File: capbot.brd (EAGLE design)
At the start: 48.3 x 49 mm, 67 parts, among them J1 USBPCB, J2 USBPCB, J3 USBPCB

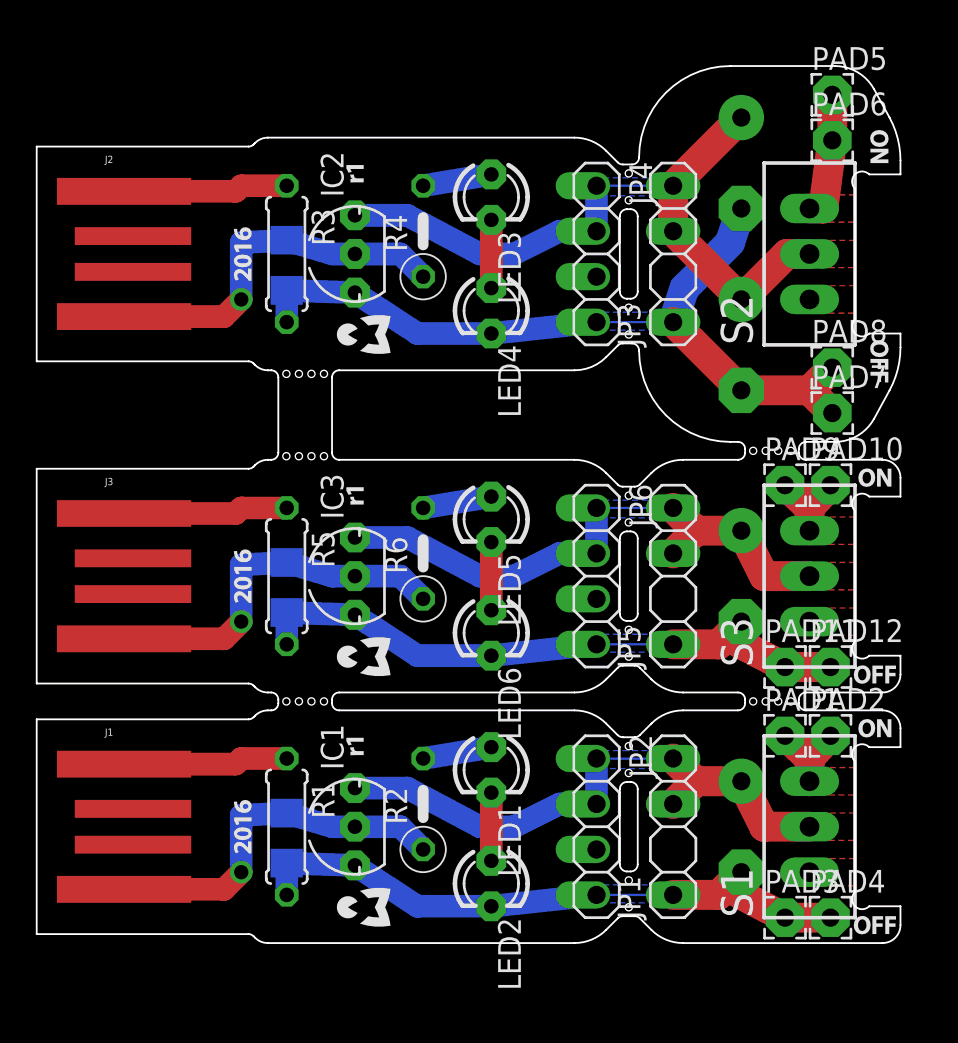
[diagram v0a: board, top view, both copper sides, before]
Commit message: Add power LED function.
With one added Zener diode, the top LED indicates that the device is powered, while both LEDs together still indicate that charging is completed.
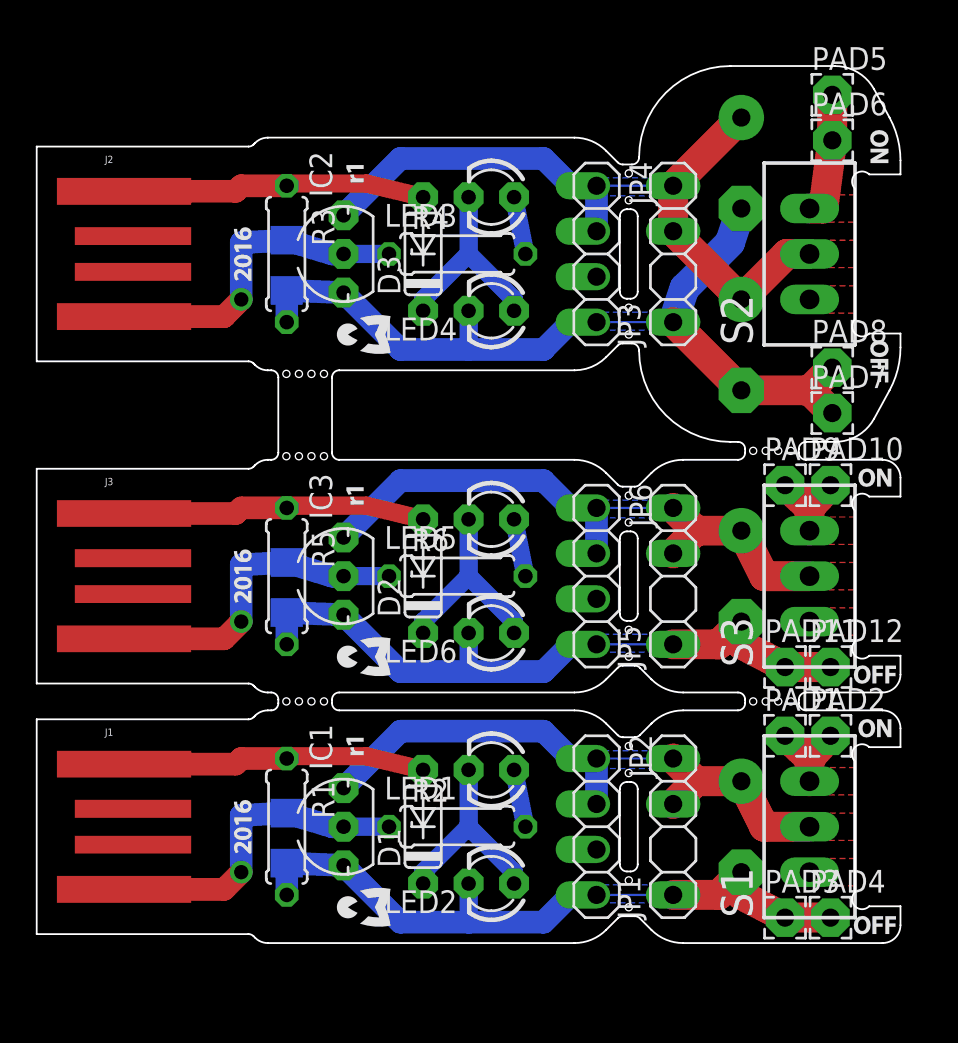
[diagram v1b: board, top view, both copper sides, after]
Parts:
- added D1, D2, D3: BZX55/6, cwpackage:DO35Z6
- R2, R4, R6: device resistor:0207/5V -> resistor:0207/7
- moved R4 2.29 mm to (23.5, 38.5), turned to 0 degrees
- moved R2 2.29 mm to (23.5, 6.50), turned to 0 degrees
- moved R6 2.29 mm to (23.5, 20.5), turned to 0 degrees
- moved IC1 0.64 mm to (17.1, 6.50)
- moved IC2 0.64 mm to (17.1, 38.5)
- moved IC3 0.64 mm to (17.1, 20.5)
- turned LED1 to 180 degrees
- turned LED2 to 180 degrees
- turned LED3 to 180 degrees
- turned LED4 to 180 degrees
- turned LED5 to 180 degrees
- turned LED6 to 180 degrees
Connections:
- net N$14: now also D3.A
- net N$19: now also D3.C
- net N$24: now also D2.A
- net N$29: now also D2.C
- net N$4: now also D1.A
- net N$9: now also D1.C
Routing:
- net N$24: track 9.22 -> 17.1 mm
- net N$4: track 9.22 -> 17.1 mm
- net N$14: track 9.22 -> 17.1 mm
- net N$9: track 3.81 -> 11.6 mm
- net N$29: track 3.81 -> 11.6 mm
- net N$19: track 3.81 -> 11.6 mm
- net N$11: track 44.5 -> 47.9 mm
- net N$1: track 35.0 -> 38.4 mm
- net N$21: track 35.0 -> 38.4 mm
- net N$26: track 20.9 -> 18.5 mm
- net N$6: track 20.9 -> 18.5 mm
- net N$16: track 20.9 -> 18.5 mm
- net N$22: track 32.7 -> 34.4 mm
- net N$2: track 32.7 -> 34.4 mm
- net N$12: track 39.3 -> 41.1 mm
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
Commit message: Get rid of a via by using an existing hole, and some other prettifications.
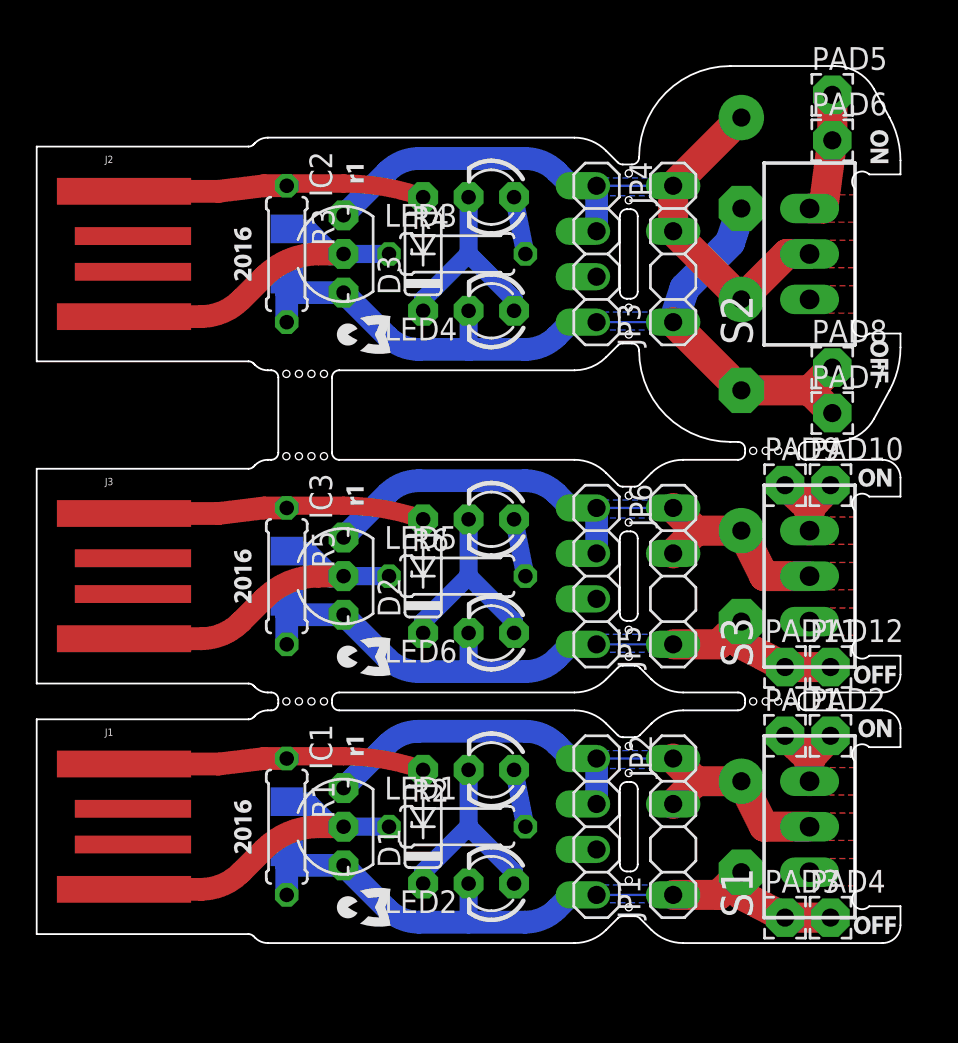
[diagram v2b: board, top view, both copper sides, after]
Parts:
- moved C7 0.64 mm to (14.0, 20.5)
- moved C2 0.63 mm to (14.0, 6.50)
- moved C4 0.63 mm to (14.0, 38.5)
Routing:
- net N$6: track 18.5 -> 20.3 mm, vias 1 -> 0
- net N$21: track 38.4 -> 39.4 mm
- net N$11: track 47.9 -> 48.9 mm
- net N$1: track 38.4 -> 39.4 mm
- net N$16: track 18.5 -> 19.5 mm, vias 1 -> 0
- net N$26: track 18.5 -> 19.5 mm, vias 1 -> 0

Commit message: Replace the zero-line-width silkscreen polygons by ones made for 0.15 mm line width.
Previously, they needlessly inflated the Gerber file size because Eagle apparently uses lines of the same width as the outline to fill them, resulting in ten-thousands of zero-width lines. The manufacturing also used a greater width (probably 0.15 mm), expanding the shapes.
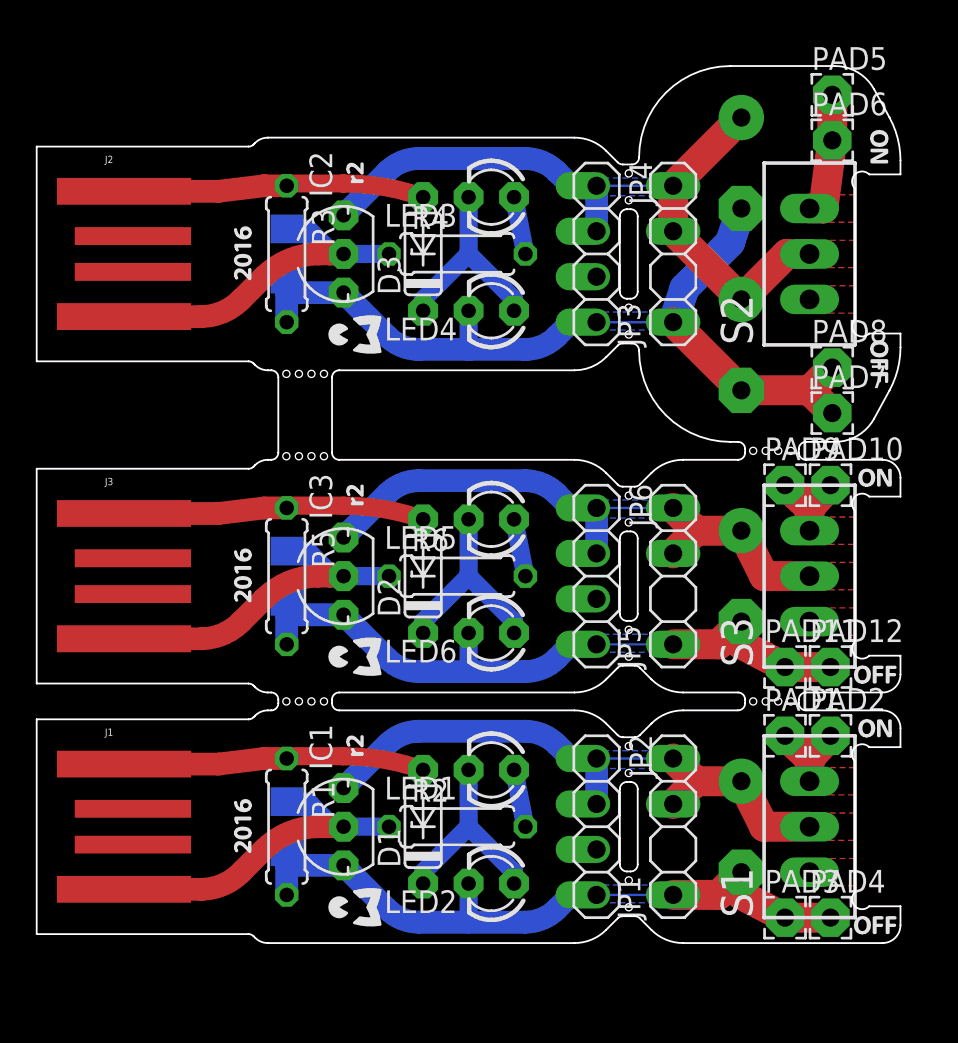
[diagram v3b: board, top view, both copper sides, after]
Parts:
- removed U$10, U$4, U$6: (no value), cwlogo:R1
- added U$22, U$23, U$24: (no value), cwlogo:R2
- moved U$1 0.49 mm to (17.8, 34.0)
- moved U$2 0.49 mm to (17.8, 2.00)
- moved U$8 0.49 mm to (17.8, 16.0)
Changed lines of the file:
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@@
 <element name="J2" library="SparkFun-Connectors" package="USB-A-PCB" value="USBPCB" x="5.08" y="38.5"/>
 <element name="C5" library="resistor" package="E5-10,5" value="" x="39.37" y="43.58" rot="MR270"/>
-<element name="U$1" library="cwlogo" package="CWLOGO-3" value="" x="18.27" y="34" rot="R90"/>
-<element name="U$2" library="cwlogo" package="CWLOGO-3" value="" x="18.27" y="2" rot="R90"/>
+<element name="U$1" library="cwlogo" package="CWLOGO-3" value="" x="17.78" y="34" rot="R90"/>
+<element name="U$2" library="cwlogo" package="CWLOGO-3" value="" x="17.78" y="2" rot="R90"/>
 <element name="U$3" library="cwlogo" package="2016" value="" x="12" y="6.5" rot="R90"/>
-<element name="U$4" library="cwlogo" package="R1" value="" x="18.27" y="11" rot="R90"/>
 <element name="U$5" library="cwlogo" package="2016" value="" x="12" y="38.5" rot="R90"/>
-<element name="U$6" library="cwlogo" package="R1" value="" x="18.27" y="43" rot="R90"/>
 <element name="C6" library="resistor" package="E5-10,5" value="" x="39.37" y="20.5" rot="MR270"/>
 <element name="S3" library="switch" package="TL3XPO" value="" x="43.18" y="20.5" rot="R90"/>
@@
 <element name="JP6" library="cwpinhead" package="1X04/OFFSETDOWN" value="" x="31.28" y="20.5" rot="R270"/>
 <element name="J3" library="SparkFun-Connectors" package="USB-A-PCB" value="USBPCB" x="5.08" y="20.5"/>
-<element name="U$8" library="cwlogo" package="CWLOGO-3" value="" x="18.27" y="16" rot="R90"/>
+<element name="U$8" library="cwlogo" package="CWLOGO-3" value="" x="17.78" y="16" rot="R90"/>
 <element name="U$9" library="cwlogo" package="2016" value="" x="12" y="20.5" rot="R90"/>
-<element name="U$10" library="cwlogo" package="R1" value="" x="18.27" y="25" rot="R90"/>
 <element name="U$7" library="cwlogo" package="OFF" value="" x="46.83" y="14.5"/>
 <element name="U$11" library="cwlogo" package="ON" value="" x="46.83" y="25.5"/>
@@
 <element name="D2" library="cwpackage" package="DO35Z6" value="BZX55/6" x="21.59" y="20.5" rot="R90"/>
 <element name="D3" library="cwpackage" package="DO35Z6" value="BZX55/6" x="21.59" y="38.5" rot="R90"/>
+<element name="U$22" library="cwlogo" package="R2" value="" x="18.27" y="11" rot="R90"/>
+<element name="U$23" library="cwlogo" package="R2" value="" x="18.27" y="25" rot="R90"/>
+<element name="U$24" library="cwlogo" package="R2" value="" x="18.27" y="43" rot="R90"/>
 </elements>
 <signals>
